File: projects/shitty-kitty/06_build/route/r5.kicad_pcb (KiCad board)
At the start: 4 copper layers, 130 x 75 mm, 82 parts, among them J1 DC-005C-20A 12V, J2 TYPE-C-31-M-12, J3 ELECTRODES INNER, J4 ELECTRODES OUTER, J5 MOTOR NEMA17, J6 ENDSTOP TERM, J8 HOST 1x6, Q1 AOD4185 revpol, SW1 TS-1187A BOOT, SW2 TS-1187A RESET, U1 ESP32-S3-WROOM-1-N8R2, U2 TMC2209-LA-T, U3 MPR121QR2 0x5A, U4 MPR121QR2 0x5B, U5 MPR121QR2 0x5C, U6 MPR121QR2 0x5D, U7 LIS2DH12TR, U8 AP63205WU-7, U9 AMS1117-3.3

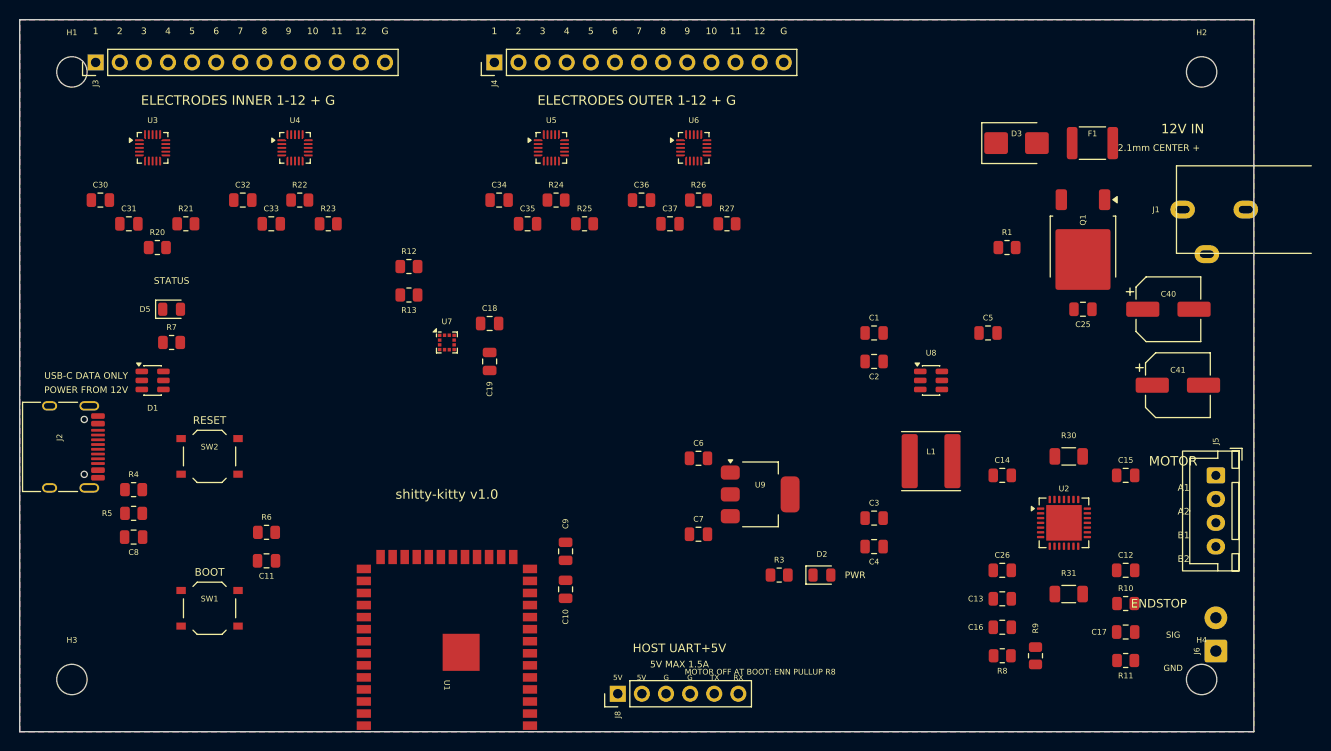
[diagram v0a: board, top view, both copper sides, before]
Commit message: shitty-kitty: routing campaign fixes — fab-floor rules (JLC 4L 3.5mil), grid-step 0.05 waves, escape-order reorder, placement round (J3 vs screw keepout, J1 edge-flush, U1 pad-edge window, J6/H4, silk de-collisions); COST_ESTIMATE + CHECKLIST drafts
Co-Authored-By: Claude Fable 5 <noreply@anthropic.com>
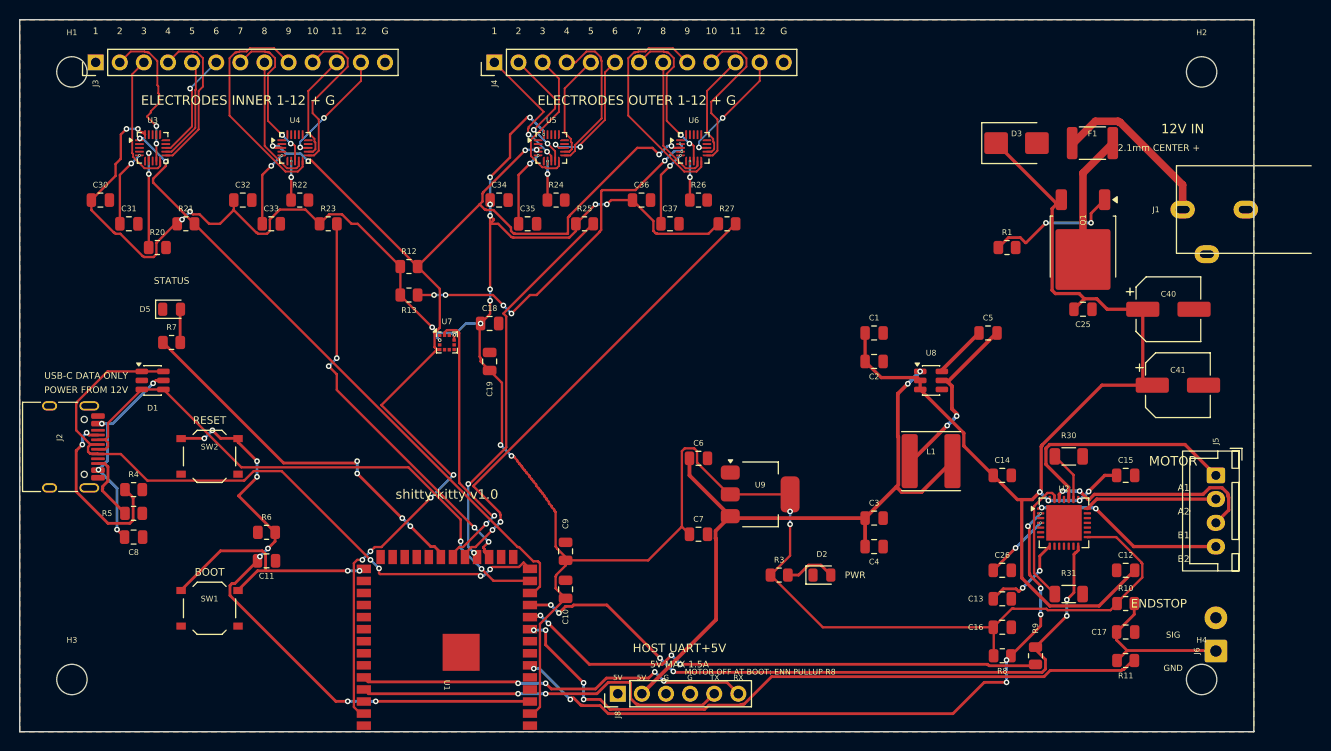
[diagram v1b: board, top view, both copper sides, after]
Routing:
- net 3V3: track 0.00 -> 281.3 mm, vias 0 -> 21
- net SDA: track 0.00 -> 128.7 mm, vias 0 -> 10
- net VIN_12V: track 0.00 -> 120.3 mm, vias 0 -> 4
- net ENN: track 0.00 -> 74.2 mm, vias 0 -> 8
- net TMC_UART: track 0.00 -> 73.2 mm, vias 0 -> 6
- net 5V: track 0.00 -> 73.1 mm, vias 0 -> 2
- net USB_DP: track 0.00 -> 71.2 mm, vias 0 -> 4
- net ENDSTOP_G: track 0.00 -> 71.1 mm, vias 0 -> 4
- net MPR_IRQ1: track 0.00 -> 67.9 mm, vias 0 -> 2
- net EN: track 0.00 -> 64.8 mm, vias 0 -> 8
- net USB_DM: track 0.00 -> 60.6 mm, vias 0 -> 2
- net TMC_TX: track 0.00 -> 56.1 mm, vias 0 -> 4
- net MPR_IRQ4: track 0.00 -> 49.5 mm, vias 0 -> 2
- net MPR_IRQ2: track 0.00 -> 43.0 mm, vias 0 -> 4
- net HOST_RX: track 0.00 -> 41.7 mm, vias 0 -> 4
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
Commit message: shitty-kitty: route iteration — MPR121s rotated 90 (electrodes north/east, support south), single mega signal wave (intra-wave ripup arbitration), BRA/BRB ride the motor wave
Co-Authored-By: Claude Fable 5 <noreply@anthropic.com>
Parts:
- moved J5 7.00 mm to (176.0, 91.0)
- moved J1 6.00 mm to (166.5, 70.0)
- moved C41 5.00 mm to (167.0, 88.5)
- moved C17 4.53 mm to (166.0, 110.0)
- moved R10 4.53 mm to (166.0, 107.0)
- moved R11 4.53 mm to (166.0, 113.0)
- moved C12 3.50 mm to (170.0, 108.0)
- moved J6 3.50 mm to (176.0, 113.0)
- moved J3 3.00 mm to (61.0, 54.5)
- moved C30 2.55 mm to (61.0, 69.5)
- moved C31 2.55 mm to (64.0, 72.0)
- moved C32 2.55 mm to (76.0, 69.5)
- moved C33 2.55 mm to (79.0, 72.0)
- moved R20 2.55 mm to (67.0, 74.5)
- moved R21 2.55 mm to (70.0, 72.0)
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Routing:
- net SCL: track 39.2 -> 146.2 mm, vias 7 -> 8
- net STEP: track 0.00 -> 71.8 mm, vias 0 -> 2
- net DIAG: track 0.00 -> 68.0 mm, vias 0 -> 4
- net INDEX: track 0.00 -> 63.8 mm, vias 0 -> 4
- net USB_DP: track 71.2 -> 19.7 mm, vias 4 -> 0
- net USB_DM: track 60.6 -> 18.2 mm, vias 2 -> 4
- net 3V3: track 281.3 -> 300.0 mm, vias 21 -> 27
- net INNER10: track 17.3 -> 0.00 mm
- net INNER1: track 0.00 -> 17.1 mm, vias 0 -> 2
- net INNER7: track 16.7 -> 0.00 mm, vias 2 -> 0
- net OUTER9: track 24.3 -> 9.07 mm
- net INNER3: track 14.5 -> 0.00 mm
- net INNER9: track 24.3 -> 9.91 mm, vias 0 -> 2
- net INNER8: track 14.0 -> 0.00 mm
- net OUTER12: track 12.4 -> 26.3 mm, vias 2 -> 0
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
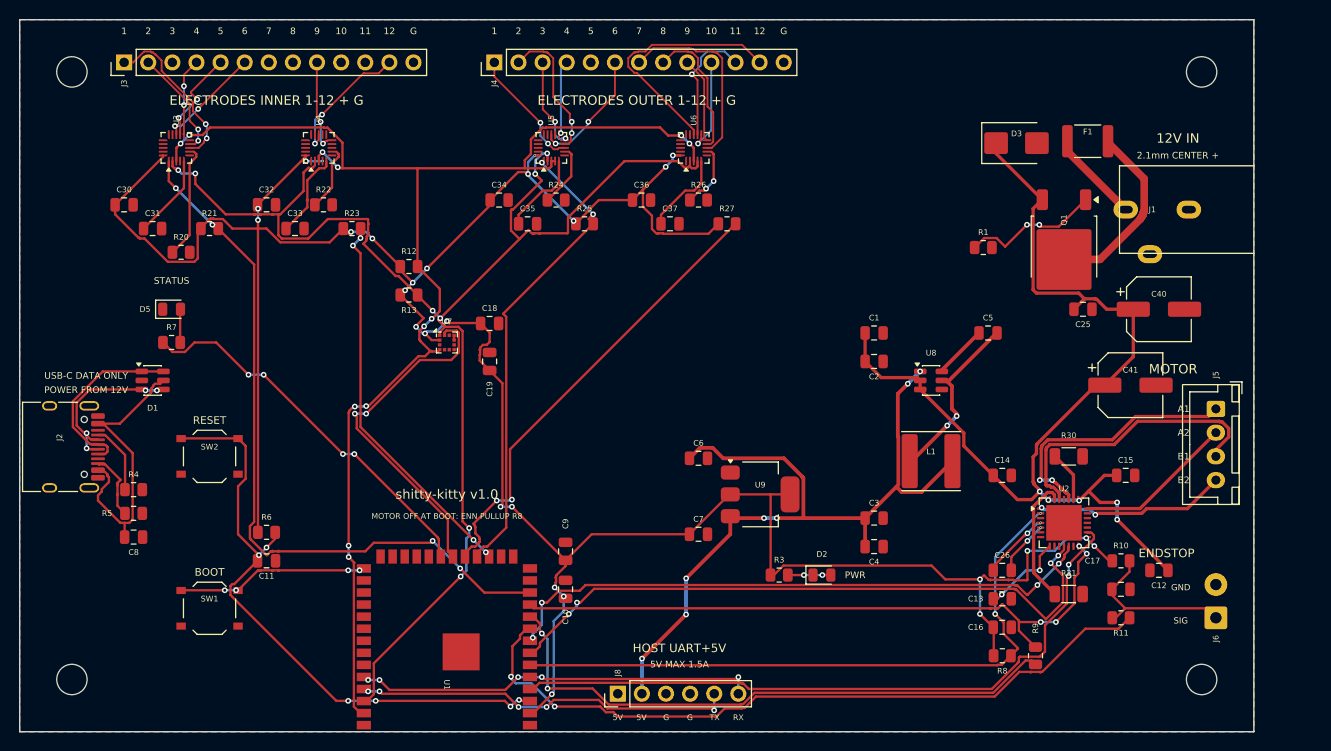
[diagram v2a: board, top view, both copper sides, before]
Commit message: shitty-kitty: fab-floor pin for KRT (no advanced-via escalation), honest hole floors (h2h 0.3/holeclr 0.2), ELEC/3V3 width floors match router grading, route_surgery tool, stitcher fine-pitch GND rescue + via-pad joins
Co-Authored-By: Claude Fable 5 <noreply@anthropic.com>
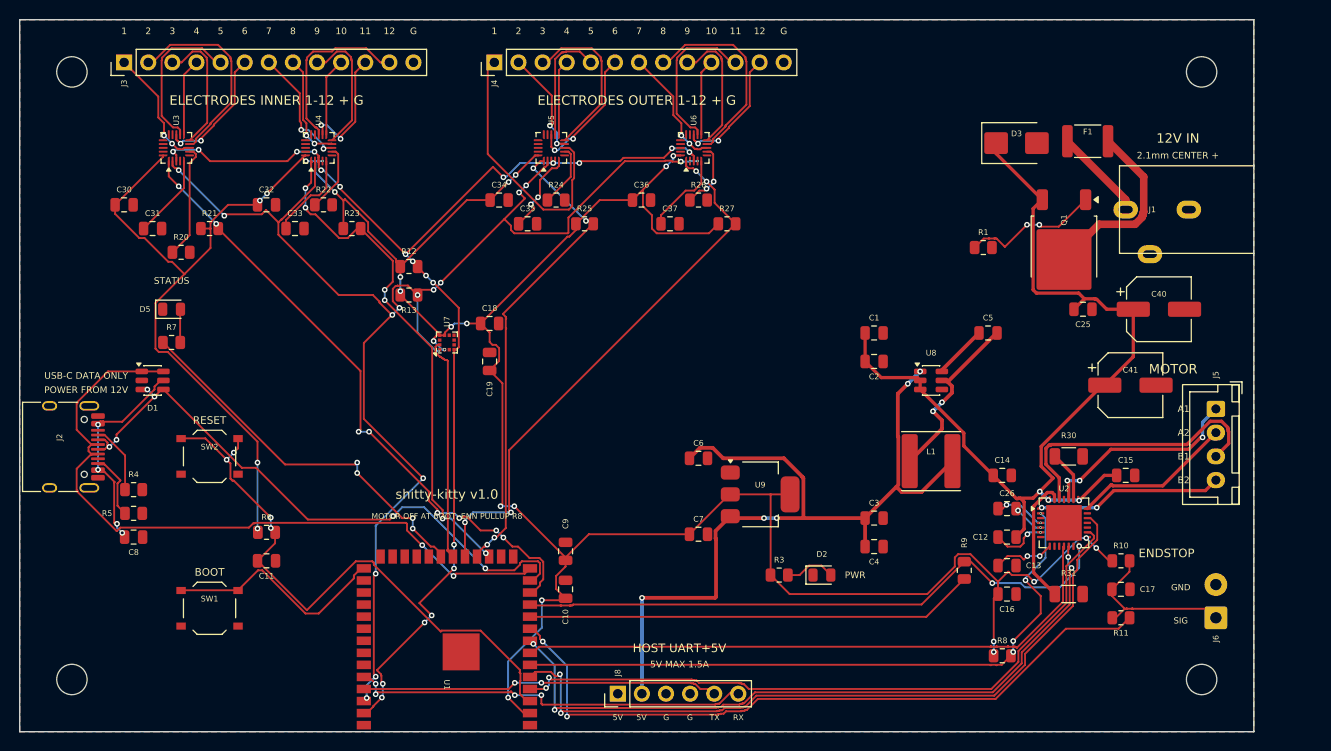
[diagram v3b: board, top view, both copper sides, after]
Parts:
- moved C12 16.4 mm to (154.0, 104.5)
- moved R9 11.7 mm to (149.5, 108.0)
- moved C26 6.52 mm to (154.0, 101.5)
- moved C13 3.54 mm to (154.0, 107.5)
- moved C16 3.54 mm to (154.0, 110.5)
- turned U7 to 90 degrees
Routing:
- net DIR: track 0.00 -> 77.9 mm, vias 0 -> 2
- net USB_DP: track 19.7 -> 75.6 mm, vias 0 -> 2
- net USB_DM: track 18.2 -> 64.7 mm, vias 4 -> 6
- net TMC_TX: track 62.7 -> 47.4 mm, vias 2 -> 0
- net OUTER1: track 13.0 -> 27.2 mm, vias 2 -> 0
- net SDA: track 139.8 -> 125.7 mm, vias 12 -> 21
- net INNER3: track 0.00 -> 13.8 mm
- net ACC_INT: track 37.0 -> 23.7 mm, vias 2 -> 0
- net MPR_IRQ2: track 40.9 -> 54.2 mm, vias 4 -> 6
- net INNER11: track 0.00 -> 12.8 mm, vias 0 -> 2
- net OUTER12: track 26.3 -> 13.5 mm, vias 0 -> 2
- net INNER7: track 0.00 -> 12.7 mm, vias 0 -> 2
- net OUTER5: track 0.00 -> 12.5 mm
- net INNER8: track 0.00 -> 11.4 mm, vias 0 -> 2
- net INDEX: track 63.8 -> 74.3 mm
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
